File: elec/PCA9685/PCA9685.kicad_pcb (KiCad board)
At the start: 2 copper layers, 17 parts, among them J1 Conn_bat_power, J10 Servo 2.3, J2 I2C_main_card, J3 Servo 1.1, J4 Servo 1.2, J5 Servo 1.3, J6 Servo Flag, J7 Servo Manche, J8 Servo 2.1, J9 Servo 2.2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

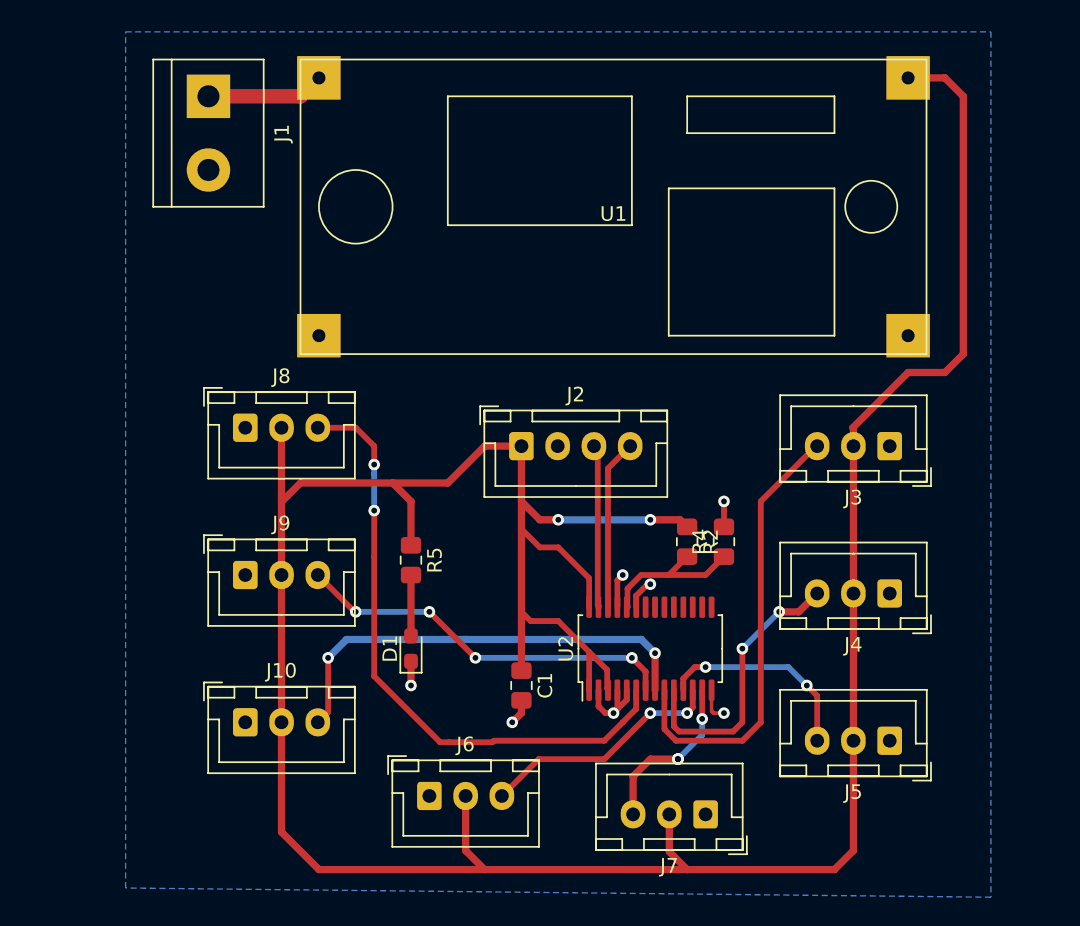
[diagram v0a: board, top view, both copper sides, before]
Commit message: Carte PCA9695 V2 : piste plus large, meilleur routage, texte au bon endroit et ajout des trous Carte Principale : Patch du texte, récupération d'une dizaine de mm sur un côté
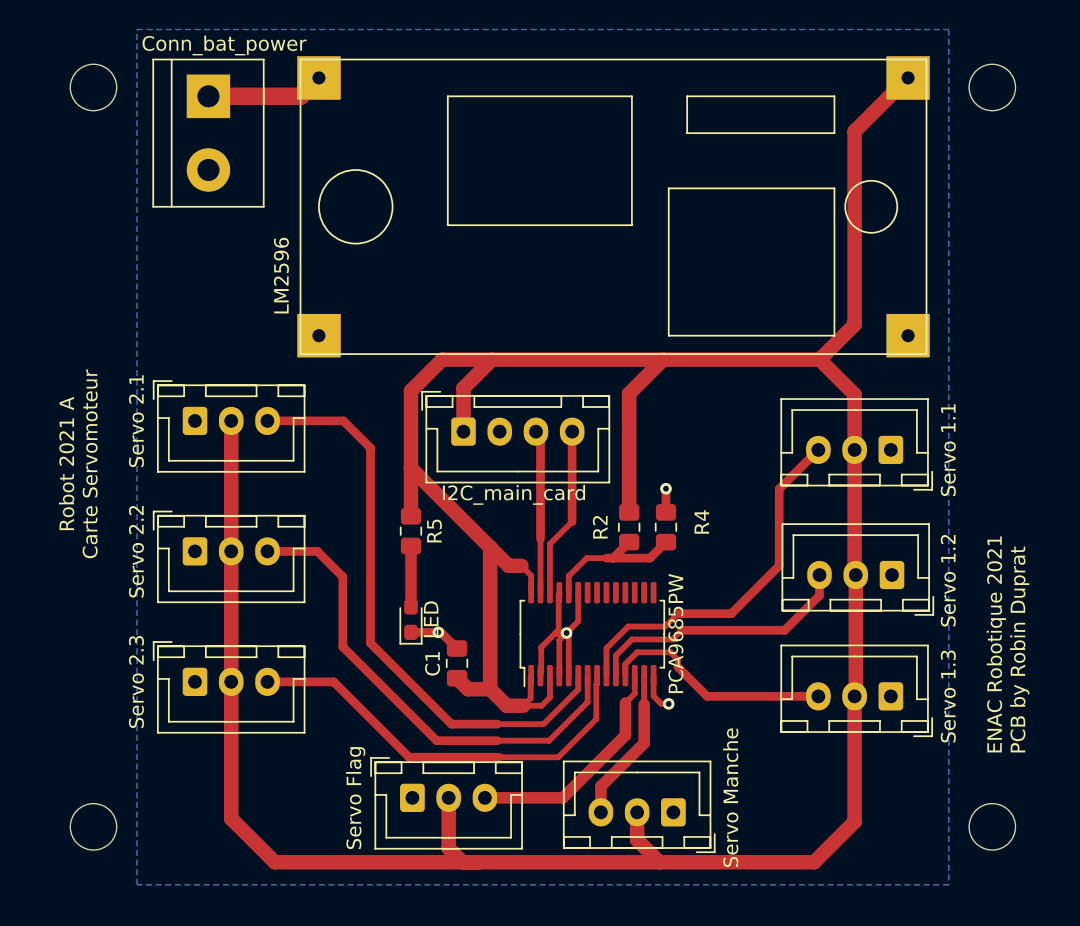
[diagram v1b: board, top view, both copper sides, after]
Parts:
- added REF**: MountingHole_3.2mm_M3, MountingHole:MountingHole_3.2mm_M3, F.Cu at (67.0, 54.0)
- added REF**: MountingHole_3.2mm_M3, MountingHole:MountingHole_3.2mm_M3, F.Cu at (67.0, 105.0)
- added REF**: MountingHole_3.2mm_M3, MountingHole:MountingHole_3.2mm_M3, F.Cu at (129.0, 105.0)
- added REF**: MountingHole_3.2mm_M3, MountingHole:MountingHole_3.2mm_M3, F.Cu at (129.0, 54.0)
- moved C1 4.70 mm to (92.1, 93.7), turned to 90 degrees
- moved J10 4.45 mm to (74.0, 95.0)
- moved J2 4.12 mm to (92.5, 77.7)
- moved R2 4.12 mm to (104.0, 84.3)
- moved R4 4.12 mm to (106.5, 84.3)
- moved U2 4.12 mm to (101.4, 91.7)
- moved J9 3.83 mm to (74.0, 86.0)
- moved J8 3.50 mm to (74.0, 77.0)
- moved J5 3.06 mm to (122.0, 96.0)
- moved J7 2.22 mm to (107.0, 104.0)
- moved D1 2.00 mm to (88.9, 90.7)
- moved R5 2.00 mm to (88.9, 84.6)
- moved J4 1.28 mm to (122.1, 87.6)
- moved J6 1.18 mm to (89.0, 103.0)
- moved J3 0.27 mm to (122.0, 79.0)
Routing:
- net +5V: track 210.2 -> 226.4 mm, vias 2 -> 0
- net GND: track 18.0 -> 24.7 mm, vias 7 -> 4
- net /servo2.2: track 26.7 -> 33.3 mm, vias 4 -> 0
- net /servo1.1: track 30.9 -> 25.3 mm
- net /servo2.1: track 42.5 -> 39.9 mm, vias 2 -> 0
- net /servo2.3: track 30.8 -> 29.1 mm, vias 2 -> 0
- net /servo1.3: track 14.4 -> 16.0 mm, vias 2 -> 0
- net /servoFlag: track 16.9 -> 15.9 mm, vias 2 -> 0
- net /servoManche: track 11.7 -> 10.7 mm, vias 3 -> 0
- net /servo1.2: track 19.5 -> 18.6 mm, vias 2 -> 0
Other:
- board text added: "ENAC Robotique 2021 PCB by Robin Duprat"
- board text added: "Robot 2021 A Carte Servomoteur"

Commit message: Carte Principale : 99mm de long !!!
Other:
- board outline added: 70 x 59 mm
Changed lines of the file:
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@@
   (general
     (thickness 1.6)
-    (drawings 6)
+    (drawings 8)
     (tracks 157)
     (zones 0)
@@
     )
   )
+  (dimension 59 (width 0.15) (layer Dwgs.User)
+    (gr_text "59,000 mm" (at 140.3 79.5 90) (layer Dwgs.User)
+      (effects (font (size 1 1) (thickness 0.15)))
+    )
+    (feature1 (pts (xy 133 50) (xy 139.586421 50)))
+    (feature2 (pts (xy 133 109) (xy 139.586421 109)))
+    (crossbar (pts (xy 139 109) (xy 139 50)))
+    (arrow1a (pts (xy 139 50) (xy 139.586421 51.126504)))
+    (arrow1b (pts (xy 139 50) (xy 138.413579 51.126504)))
+    (arrow2a (pts (xy 139 109) (xy 139.586421 107.873496)))
+    (arrow2b (pts (xy 139 109) (xy 138.413579 107.873496)))
+  )
+  (dimension 70 (width 0.15) (layer Dwgs.User)
+    (gr_text "70,000 mm" (at 98 113.3) (layer Dwgs.User)
+      (effects (font (size 1 1) (thickness 0.15)))
+    )
+    (feature1 (pts (xy 63 109) (xy 63 112.586421)))
+    (feature2 (pts (xy 133 109) (xy 133 112.586421)))
+    (crossbar (pts (xy 133 112) (xy 63 112)))
+    (arrow1a (pts (xy 63 112) (xy 64.126504 111.413579)))
+    (arrow1b (pts (xy 63 112) (xy 64.126504 112.586421)))
+    (arrow2a (pts (xy 133 112) (xy 131.873496 111.413579)))
+    (arrow2b (pts (xy 133 112) (xy 131.873496 112.586421)))
+  )
+  (gr_line (start 63 109) (end 133 109) (layer Edge.Cuts) (width 0.05))
+  (gr_line (start 63 50) (end 63 109) (layer Edge.Cuts) (width 0.05))
+  (gr_line (start 133 50) (end 63 50) (layer Edge.Cuts) (width 0.05))
+  (gr_line (start 133 109) (end 133 50) (layer Edge.Cuts) (width 0.05))
   (gr_text "ENAC Robotique 2021\nPCB by Robin Duprat" (at 130 100 90) (layer F.SilkS)
     (effects (font (size 1 1) (thickness 0.15)) (justify left))
@@
     (effects (font (size 1 1) (thickness 0.15)))
   )
-  (gr_line (start 133 109) (end 133 50) (layer Dwgs.User) (width 0.15))
-  (gr_line (start 63 109) (end 133 109) (layer Dwgs.User) (width 0.15))
-  (gr_line (start 63 50) (end 63 109) (layer Dwgs.User) (width 0.15))
-  (gr_line (start 133 50) (end 63 50) (layer Dwgs.User) (width 0.15))
   (segment (start 106.49 83.31) (end 106.49 81.677) (width 0.6) (layer F.Cu) (net 1))
   (segment (start 106.49 81.677) (end 106.49 81.677) (width 0.6) (layer F.Cu) (net 1))

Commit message: Tentative de logo ENAC : echec Mise à jour visuelle, finission des cadres et plan de masse
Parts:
- D1: value LED -> LED PWR
- moved J1 6.39 mm to (74.9, 61.0)
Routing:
- net +12V: track 8.15 -> 15.3 mm
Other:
- board text added: "GND"

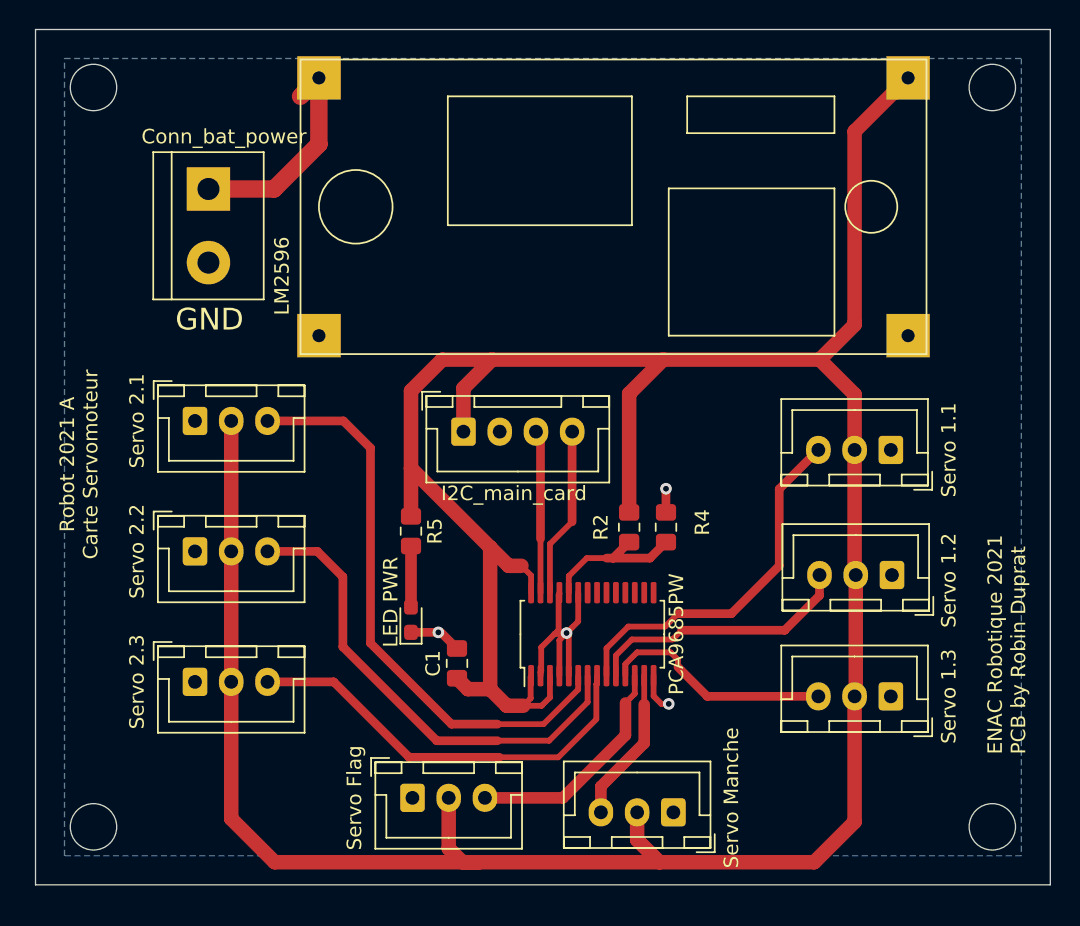
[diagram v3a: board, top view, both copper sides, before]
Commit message: Patch footprint connecteurs servo sur carte PAC9685
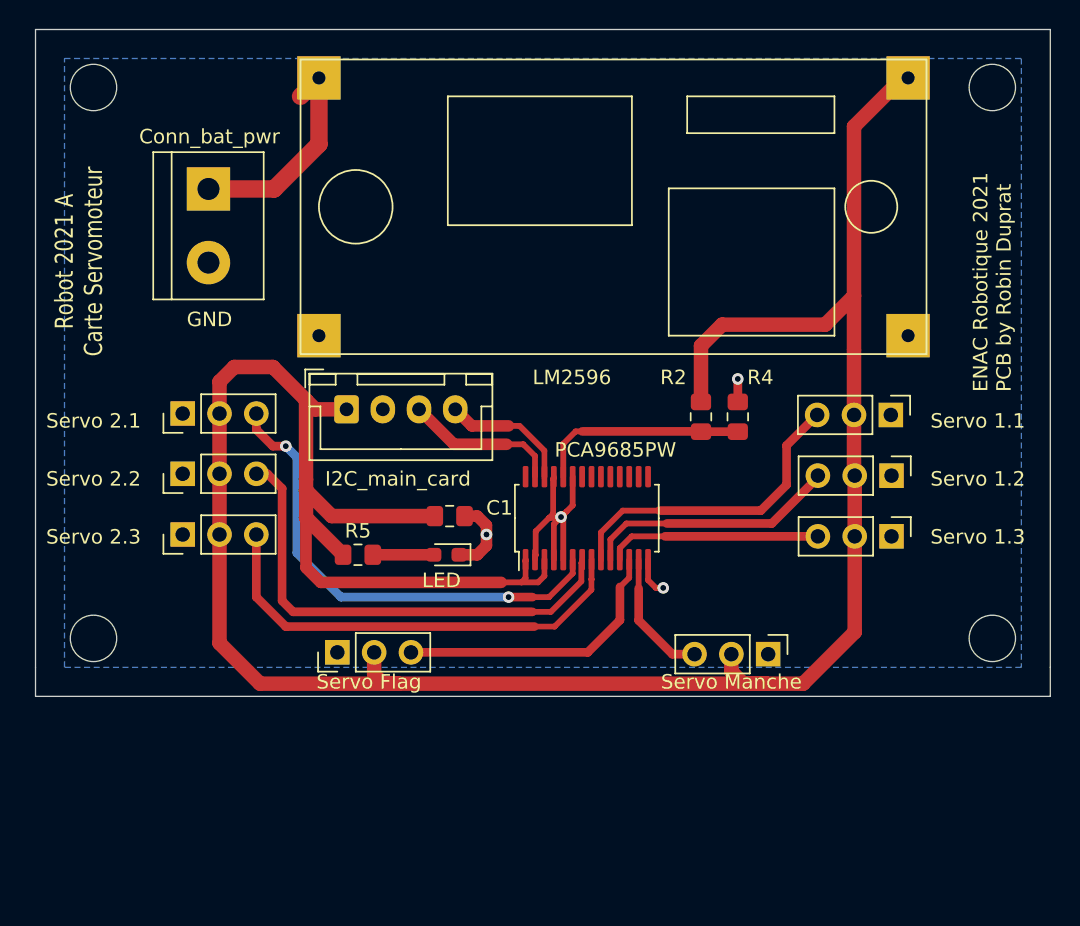
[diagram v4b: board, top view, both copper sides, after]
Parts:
- D1: value LED PWR -> LED
- J1: value Conn_bat_power -> Conn_bat_pwr
- J10, J3, J4, J5, J6, J7, J8, J9: footprint Connector_JST:JST_XH_B3B-XH-A_1x03_P2.50mm_Vertical -> Connector_PinHeader_2.54mm:PinHeader_1x03_P2.54mm_Vertical
- moved REF** 13.0 mm to (67.0, 92.0)
- moved REF** 13.0 mm to (129.0, 92.0)
- moved J7 12.7 mm to (113.5, 93.1), turned to 270 degrees
- moved J6 11.3 mm to (83.8, 93.0), turned to 90 degrees
- moved J5 11.0 mm to (122.0, 85.0), turned to 270 degrees
- moved J10 10.2 mm to (73.2, 84.8), turned to 90 degrees
- moved C1 10.2 mm to (91.6, 83.6), turned to 0 degrees
- moved R2 9.09 mm to (108.9, 76.7)
- moved R4 9.09 mm to (111.4, 76.7)
- moved J2 8.21 mm to (84.5, 76.2)
- moved U2 8.01 mm to (101.0, 83.7)
- moved J4 6.86 mm to (122.0, 80.8), turned to 270 degrees
- moved J9 5.42 mm to (73.2, 80.6), turned to 90 degrees
- moved D1 5.10 mm to (91.3, 86.2), turned to 180 degrees
- moved R5 4.01 mm to (85.2, 86.2), turned to 0 degrees
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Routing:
- net +5V: track 226.4 -> 183.4 mm
- net /servo2.1: track 39.9 -> 33.2 mm, vias 0 -> 2
- net Net-(R2-Pad2): track 10.4 -> 14.7 mm
- net /servoFlag: track 15.9 -> 19.8 mm
- net /servo1.1: track 25.3 -> 21.7 mm
- net /SCL: track 11.7 -> 9.12 mm
- net /servo2.3: track 29.1 -> 31.4 mm
- net /servoManche: track 10.7 -> 9.01 mm
- net GND: track 24.7 -> 26.4 mm
- net /servo1.3: track 16.0 -> 14.8 mm
- net /SDA: track 11.7 -> 10.8 mm
- net /servo1.2: track 18.6 -> 17.6 mm
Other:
- board size 70 x 59 mm -> 70 x 46 mm

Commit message: Mise à jour espacement connecteur servo sur carte PCA9685
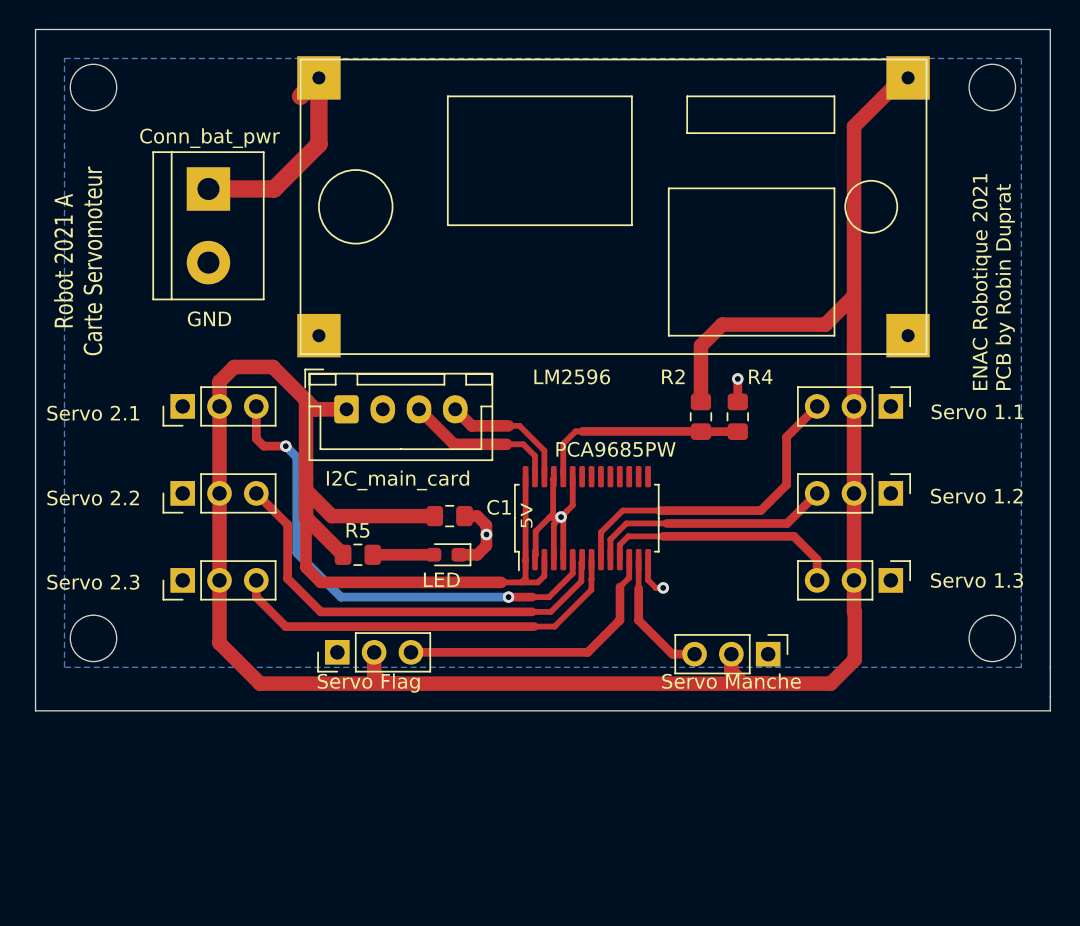
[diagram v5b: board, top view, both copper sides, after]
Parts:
- moved J10 3.16 mm to (73.2, 88.0)
- moved J5 3.04 mm to (122.0, 88.0)
- moved J9 1.36 mm to (73.2, 82.0)
- moved J4 1.23 mm to (122.0, 82.0)
- moved J3 0.59 mm to (122.0, 76.0)
- moved J8 0.49 mm to (73.2, 76.0)
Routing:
- net +5V: track 183.4 -> 190.1 mm
- net /servo2.3: track 31.4 -> 28.2 mm
- net /servo2.2: track 33.3 -> 30.4 mm
- net /servo1.3: track 14.8 -> 17.0 mm
- net /servo2.1: track 33.2 -> 34.1 mm
- net /servo1.2: track 17.6 -> 17.0 mm
- net /servo1.1: track 21.7 -> 22.3 mm
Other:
- board size 70 x 46 mm -> 70 x 47 mm
- board text added: "5V"

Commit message: Final push
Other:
- board text removed: "5V"
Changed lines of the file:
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@@
   (general
     (thickness 1.6)
-    (drawings 14)
+    (drawings 25)
     (tracks 168)
     (zones 0)
@@
       (plotvalue true)
       (plotinvisibletext false)
-      (padsonsilk false)
+      (padsonsilk true)
       (subtractmaskfromsilk false)
       (outputformat 1)
       (mirror false)
-      (drillshape 1)
+      (drillshape 0)
       (scaleselection 1)
-      (outputdirectory ""))
+      (outputdirectory "gerbers/"))
   )
   (net 0 "")
@@
     )
   )
-  (dimension 70 (width 0.15) (layer Dwgs.User)
-    (gr_text "70,000 mm" (at 98 102.3) (layer Dwgs.User)
-      (effects (font (size 1 1) (thickness 0.15)))
-    )
-    (feature1 (pts (xy 63 97) (xy 63 101.586421)))
-    (feature2 (pts (xy 133 97) (xy 133 101.586421)))
-    (crossbar (pts (xy 133 101) (xy 63 101)))
-    (arrow1a (pts (xy 63 101) (xy 64.126504 100.413579)))
-    (arrow1b (pts (xy 63 101) (xy 64.126504 101.586421)))
-    (arrow2a (pts (xy 133 101) (xy 131.873496 100.413579)))
-    (arrow2b (pts (xy 133 101) (xy 131.873496 101.586421)))
-  )
+  (gr_circle (center 96.774 87.884) (end 96.774 88.138) (layer F.SilkS) (width 0.12))
+  (gr_line (start 83.82 91.186) (end 83.82 90.17) (layer F.SilkS) (width 0.12))
+  (gr_line (start 113.792 90.932) (end 113.792 89.916) (layer F.SilkS) (width 0.12))
+  (gr_text "GND\n" (at 122.174 91.948) (layer F.SilkS)
+    (effects (font (size 1 1) (thickness 0.15)))
+  )
+  (gr_line (start 122.174 89.916) (end 122.174 90.932) (layer F.SilkS) (width 0.12))
+  (gr_line (start 122.174 84.074) (end 122.174 86.106) (layer F.SilkS) (width 0.12))
+  (gr_line (start 122.174 77.978) (end 122.174 80.01) (layer F.SilkS) (width 0.12))
+  (gr_line (start 122.174 73.152) (end 122.174 73.914) (layer F.SilkS) (width 0.12))
+  (gr_text GND (at 73.025 92.329) (layer F.SilkS)
+    (effects (font (size 1 1) (thickness 0.15)))
+  )
+  (gr_line (start 73.025 90.043) (end 73.025 91.186) (layer F.SilkS) (width 0.12))
+  (gr_line (start 73.025 84.074) (end 73.025 86.106) (layer F.SilkS) (width 0.12))
+  (gr_line (start 73.025 78.232) (end 73.025 80.01) (layer F.SilkS) (width 0.12))
+  (gr_line (start 73.025 72.517) (end 73.025 73.914) (layer F.SilkS) (width 0.12))
   (dimension 47 (width 0.15) (layer Dwgs.User)
     (gr_text "47,000 mm" (at 138.3 73.5 270) (layer Dwgs.User)
@@
   (gr_line (start 63 97) (end 133 97) (layer Edge.Cuts) (width 0.05))
   (gr_line (start 63 96) (end 63 97) (layer Edge.Cuts) (width 0.05))
-  (gr_text 5V (at 96.901 83.566 90) (layer F.SilkS)
-    (effects (font (size 0.8 1) (thickness 0.2)))
-  )
   (gr_line (start 63 96) (end 63 94) (layer Edge.Cuts) (width 0.05))
   (gr_line (start 133 94) (end 133 96) (layer Edge.Cuts) (width 0.05))
